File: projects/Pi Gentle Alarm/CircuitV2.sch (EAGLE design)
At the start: 4 parts, among them X1 RASPI_BOARD_B+_E3, X2 22-23-2021

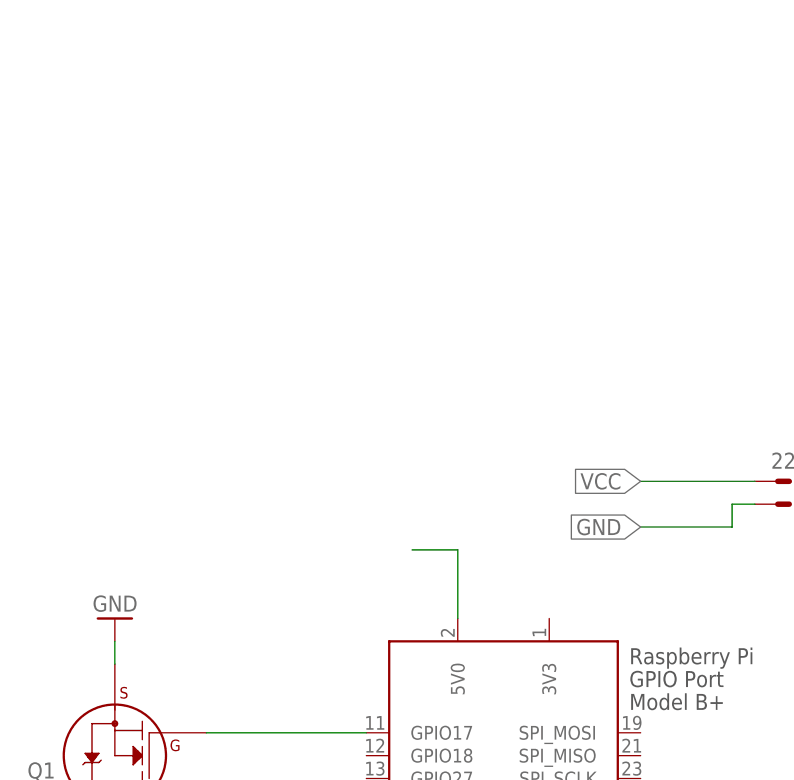
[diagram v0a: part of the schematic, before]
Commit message: Finishing steps for the hat
Added a fuse to protect the pi
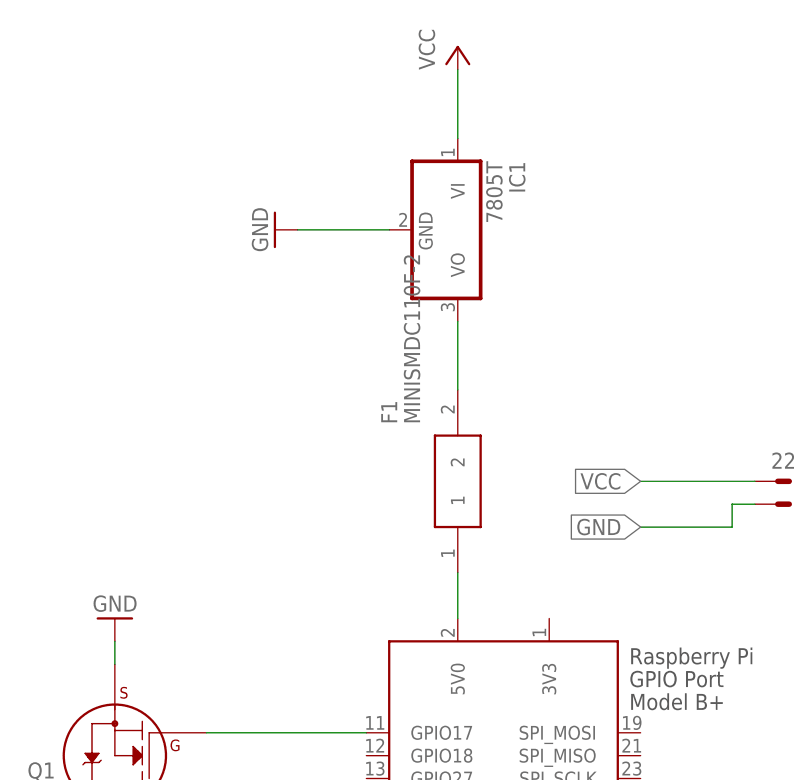
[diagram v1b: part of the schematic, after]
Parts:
- added F1: MINISMDC110F-2, MINISMDC110F-2:MINISMDC110F-2
- added IC1: 7805T, linear:7805T
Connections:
- new net N$1: F1.1, X1.5V0
- net GND: now also IC1.GND
- net N$2: now also F1.2, IC1.VO; no longer X1.5V0
- net VCC: now also IC1.VI
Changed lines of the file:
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@@
 <part name="GND1" library="supply1" library_urn="urn:adsk.eagle:library:371" deviceset="GND" device=""/>
 <part name="LED1" library="adafruit" library_urn="urn:adsk.eagle:library:420" deviceset="LED" device="SFH482" package3d_urn="urn:adsk.eagle:package:6240546/1"/>
+<part name="IC1" library="linear" library_urn="urn:adsk.eagle:library:262" deviceset="78*" device="T" package3d_urn="urn:adsk.eagle:package:16414/1" technology="05"/>
+<part name="P+2" library="supply1" library_urn="urn:adsk.eagle:library:371" deviceset="VCC" device=""/>
+<part name="GND2" library="supply1" library_urn="urn:adsk.eagle:library:371" deviceset="GND" device=""/>
+<part name="F1" library="MINISMDC110F-2" deviceset="MINISMDC110F-2" device=""/>
 </parts>
 <sheets>
@@
 <attribute name="VALUE" x="51.435" y="145.288" size="1.778" layer="96" rot="R90"/>
 </instance>
+<instance part="IC1" gate="A1" x="83.82" y="226.06" smashed="yes" rot="R270">
+<attribute name="NAME" x="89.535" y="233.68" size="1.778" layer="95" rot="R270"/>
+<attribute name="VALUE" x="86.995" y="233.68" size="1.778" layer="96" rot="R270"/>
+</instance>
+<instance part="P+2" gate="VCC" x="83.82" y="246.38" smashed="yes">
+<attribute name="VALUE" x="81.28" y="243.84" size="1.778" layer="96" rot="R90"/>
+</instance>
+<instance part="GND2" gate="1" x="63.5" y="226.06" smashed="yes" rot="R270">
+<attribute name="VALUE" x="60.96" y="228.6" size="1.778" layer="96" rot="R270"/>
+</instance>
+<instance part="F1" gate="G$1" x="83.82" y="187.96" smashed="yes" rot="R90">
+<attribute name="NAME" x="76.2" y="204.47" size="1.778" layer="95" rot="R90" align="center-left"/>
+<attribute name="VALUE" x="78.74" y="204.47" size="1.778" layer="96" rot="R90" align="center-left"/>
+</instance>
 </instances>
 <busses>
@@
 <pinref part="LED1" gate="G$1" pin="C"/>
 </segment>
+<segment>
+<pinref part="IC1" gate="A1" pin="VI"/>
+<pinref part="P+2" gate="VCC" pin="VCC"/>
+<wire x1="83.82" y1="243.84" x2="83.82" y2="236.22" width="0.1524" layer="91"/>
+</segment>
 </net>
 <net name="GND" class="0">
@@
 <pinref part="GND1" gate="1" pin="GND"/>
 <wire x1="45.72" y1="177.8" x2="45.72" y2="180.34" width="0.1524" layer="91"/>
+</segment>
+<segment>
+<pinref part="IC1" gate="A1" pin="GND"/>
+<pinref part="GND2" gate="1" pin="GND"/>
+<wire x1="66.04" y1="226.06" x2="76.2" y2="226.06" width="0.1524" layer="91"/>
 </segment>
 </net>
@@
 </segment>
 </net>
+<net name="N$1" class="0">
+<segment>
+<pinref part="X1" gate="G$1" pin="5V0"/>
+<pinref part="F1" gate="G$1" pin="1"/>
+<wire x1="83.82" y1="187.96" x2="83.82" y2="182.88" width="0.1524" layer="91"/>
+</segment>
+</net>
 <net name="N$2" class="0">
 <segment>
-<wire x1="83.82" y1="182.88" x2="83.82" y2="190.5" width="0.1524" layer="91"/>
-<wire x1="83.82" y1="190.5" x2="78.74" y2="190.5" width="0.1524" layer="91"/>
-<pinref part="X1" gate="G$1" pin="5V0"/>
+<pinref part="IC1" gate="A1" pin="VO"/>
+<pinref part="F1" gate="G$1" pin="2"/>
+<wire x1="83.82" y1="208.28" x2="83.82" y2="215.9" width="0.1524" layer="91"/>
 </segment>
 </net>
